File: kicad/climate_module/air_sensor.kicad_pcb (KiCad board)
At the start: 2 copper layers, 95 x 75 mm, 12 parts, among them U7 ATtiny1614, U8 buffer

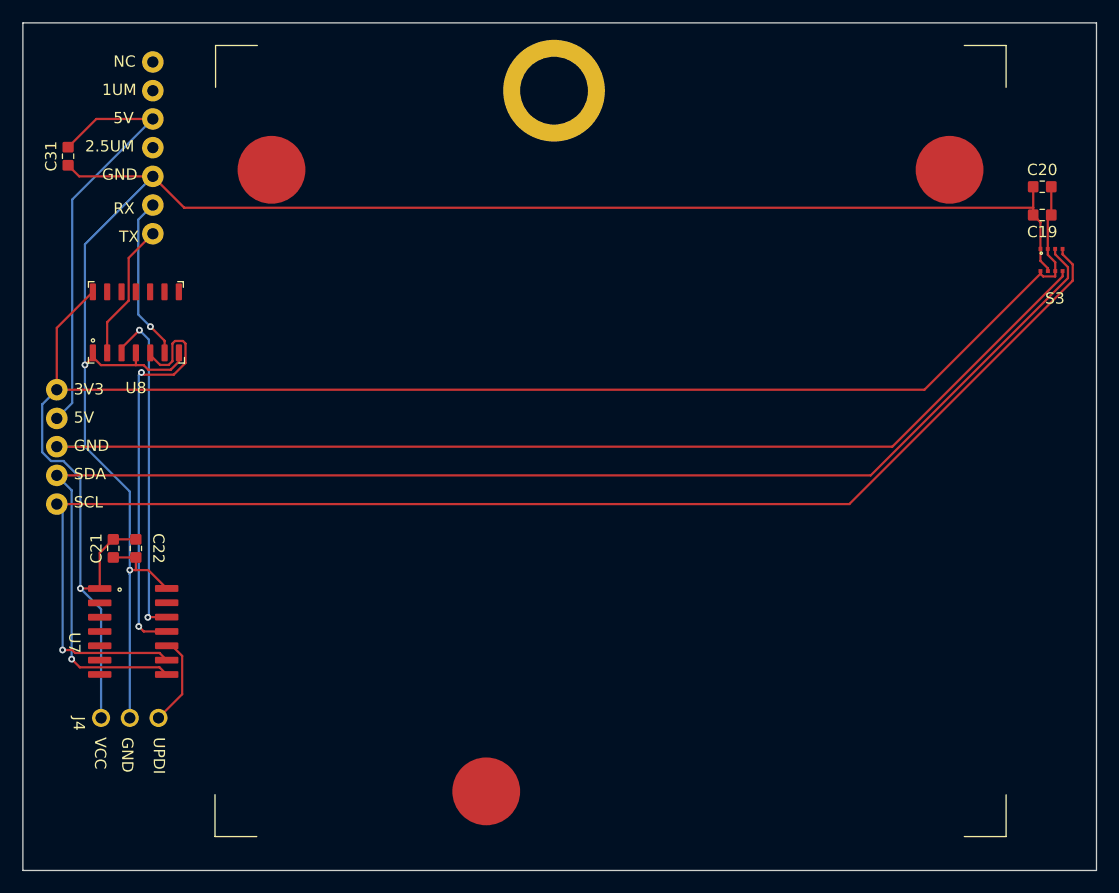
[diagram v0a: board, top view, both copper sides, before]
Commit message: added status LED to climate module
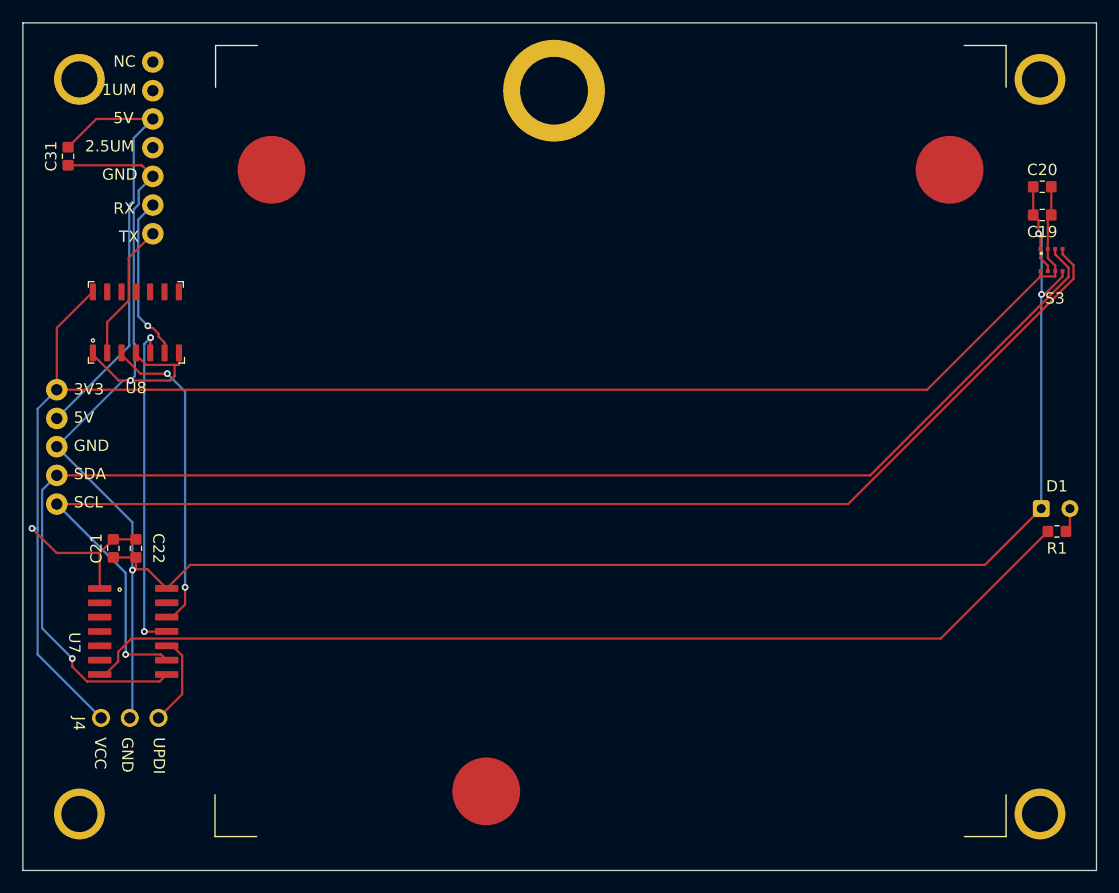
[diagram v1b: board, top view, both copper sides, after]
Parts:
- added D1: ~, common:LED_3mm_THT, F.Cu at (203.4, 112.0)
- added R1: 220, common:R_0603, F.Cu at (203.5, 111.0)
- added REF**: mounting_hole, air_sens_foots:mounting_hole, F.Cu at (116.9, 145.7)
- added REF**: mounting_hole, air_sens_foots:mounting_hole, F.Cu at (201.9, 80.7)
- added REF**: mounting_hole, air_sens_foots:mounting_hole, F.Cu at (116.9, 80.7)
- added REF**: mounting_hole, air_sens_foots:mounting_hole, F.Cu at (201.9, 145.7)
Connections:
- U7 pad 7: unconnected-(U7-TOSC2/PB2-Pad7) -> STATUS_LED
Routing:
- net STATUS_LED: track 0.00 -> 89.6 mm
- net GND: track 263.9 -> 200.1 mm, vias 2 -> 4
- net AT_CLIM_TX: track 36.9 -> 29.6 mm
- net 3V3: track 152.2 -> 157.6 mm
- net SCL: track 124.0 -> 120.9 mm
- net Net-(D1-A): track 0.00 -> 2.16 mm
- net AT_CLIM_RX: track 30.1 -> 28.1 mm
- net SDA: track 125.5 -> 127.5 mm
